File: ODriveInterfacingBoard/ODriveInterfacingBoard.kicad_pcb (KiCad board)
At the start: 2 copper layers, 144.3 x 133.7 mm, 50 parts, among them U1 ODrive, U2 MAX3077E

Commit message: Made LEDs in a Delta Configuration
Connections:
- 50W2RJ1 pad V+: Net-(50W2RJ1-Pad2) -> (no net)
- 50W2RJ1 pad V-: Net-(50W2RJ1-Pad1) -> (no net)
- Conn3 pad 1: PV+ -> /PV+
- Conn4 pad 6: +5V -> /E1_5V
- Conn4 pad 7: +3V3 -> /E1_3V3
- Conn5 pad 6: +5V -> /E0_5V
- Conn5 pad 7: +3V3 -> /E0_3V3
- D12 pad 1: GND -> M0_C
- D13 pad 1: GND -> M1_A
- D15 pad 1: GND -> M0_A
- D5 pad 1: GND -> M1_B
- D8 pad 1: GND -> M0_B
- D9 pad 1: GND -> M1_C
- R1 pad 1: Tx -> GPIO1
- R10 pad 1: PV+ -> M0_C
- R11 pad 1: PV+ -> M1_A
- R14 pad 1: PV+ -> M0_A
- R2 pad 1: Rx -> GPIO2
- R3 pad 1: PV+ -> M1_B
- R6 pad 1: PV+ -> M0_B
- R7 pad 1: PV+ -> M1_C
- U1 pad E0_3V3: +3V3 -> /E0_3V3
- U1 pad E0_5V: +5V -> /E0_5V
- U1 pad E0_GND: GND -> /E0_GND
- U1 pad E1_3V3: +3V3 -> /E1_3V3
- U1 pad E1_5V: +5V -> /E1_5V
- U1 pad E1_GND: GND -> /E1_GND
- U1 pad PV+: PV+ -> (no net)

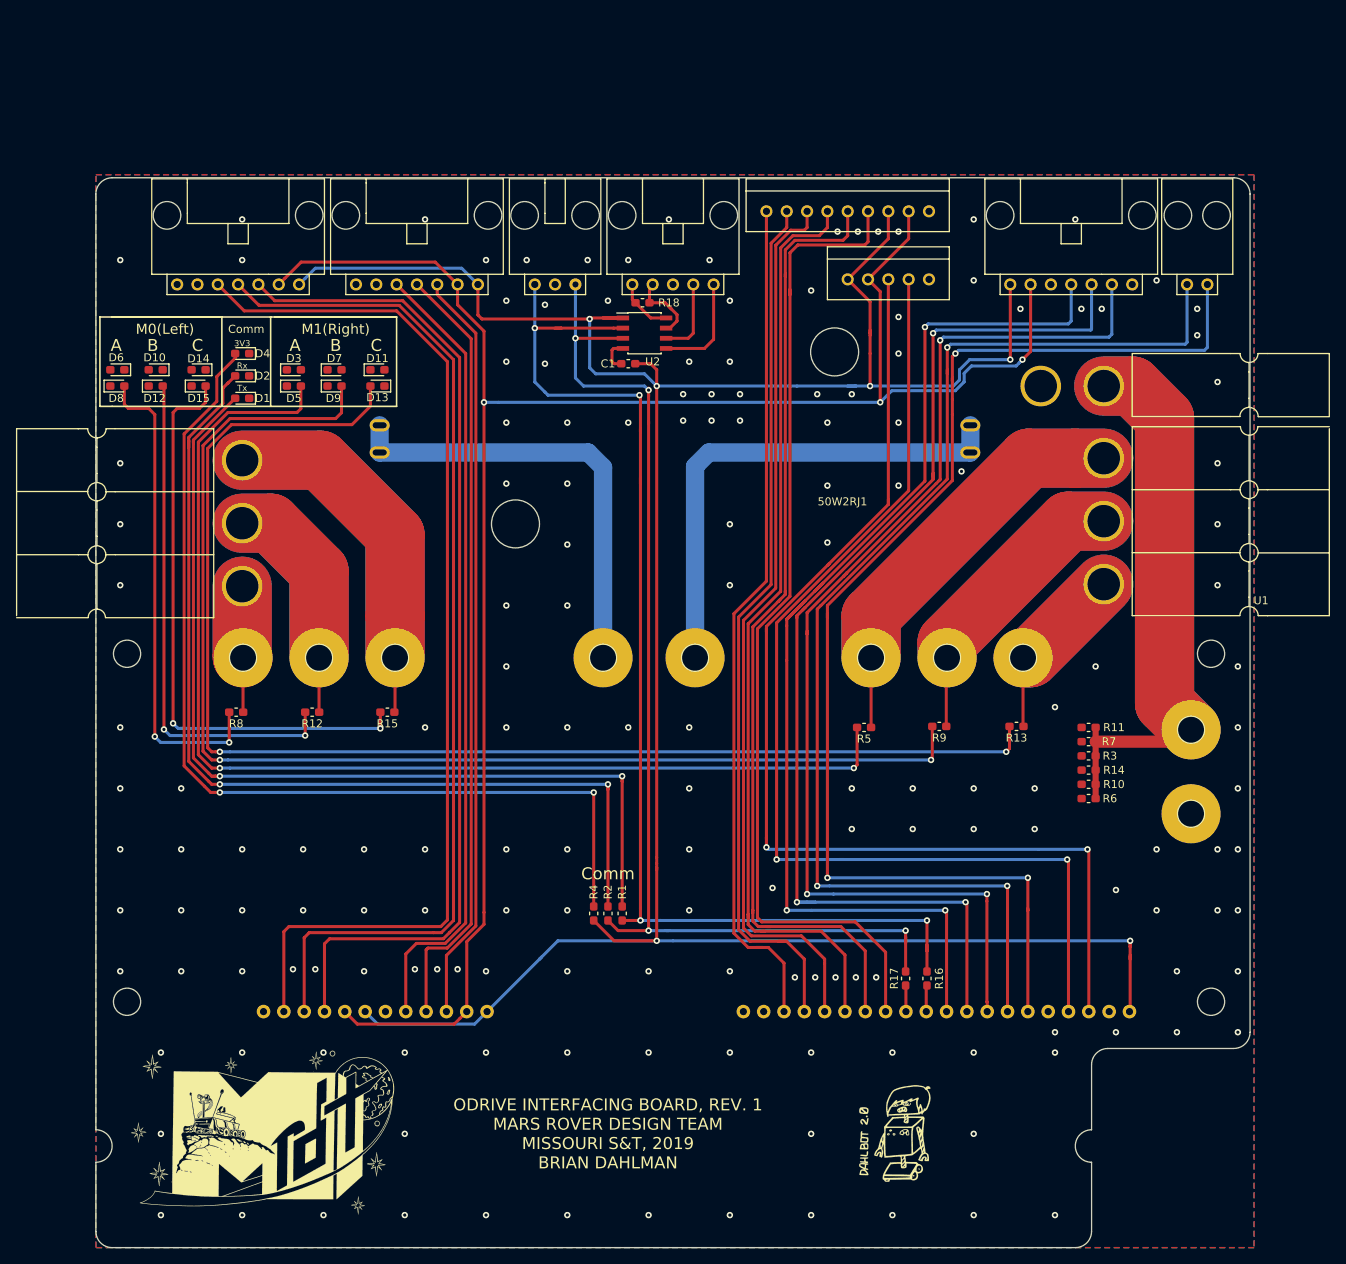
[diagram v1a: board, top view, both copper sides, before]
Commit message: Layout made, functional but needs cleaning up
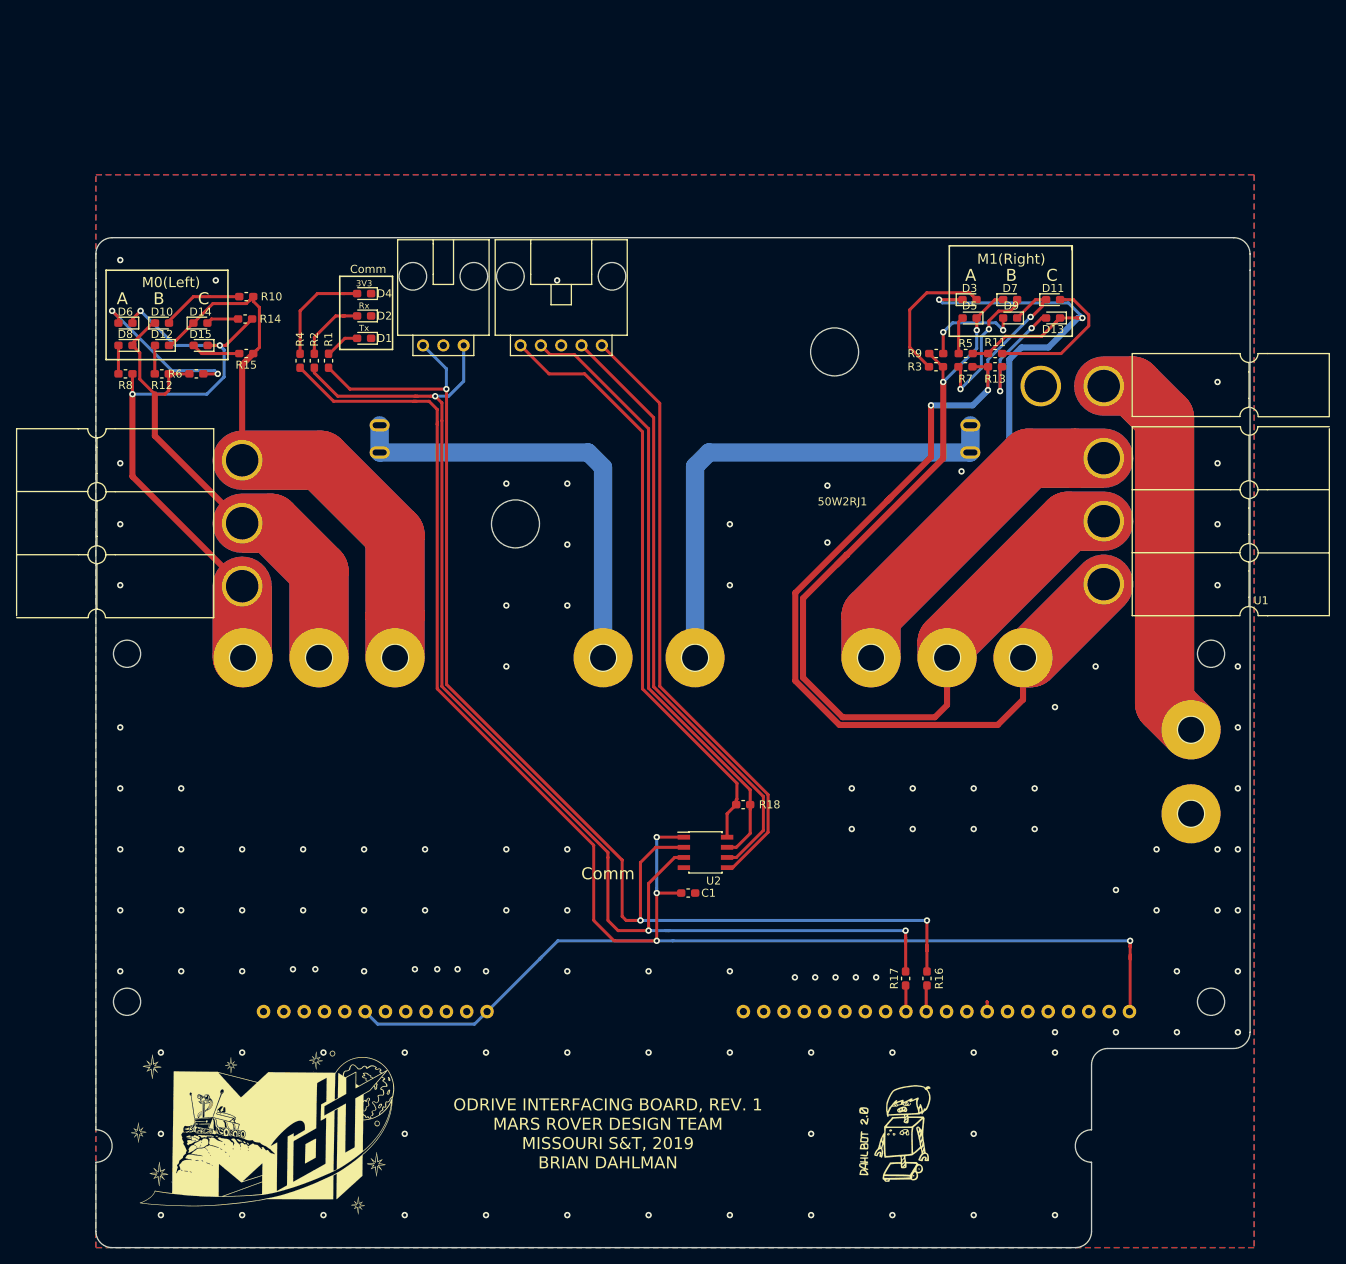
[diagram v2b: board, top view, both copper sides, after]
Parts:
- removed Conn1: Molex_SL_02, MRDT_Connectors:MOLEX_SL_02_Horizontal
- removed Conn13: Molex_SL_09, MRDT_Connectors:MOLEX_SL_09_Vertical
- removed Conn2: Molex_SL_05, MRDT_Connectors:MOLEX_SL_05_Vertical
- removed Conn4, Conn5, Conn6: Molex_SL_07, MRDT_Connectors:MOLEX_SL_07_Horizontal
- moved R6 123.5 mm to (47.6, 65.0), turned to 0 degrees
- moved R10 121.7 mm to (53.8, 55.4)
- moved R14 119.6 mm to (53.7, 58.2)
- moved D3 84.9 mm to (144.3, 55.8)
- moved D7 84.9 mm to (149.3, 55.8)
- moved D11 84.9 mm to (154.7, 55.8)
- moved D5 84.9 mm to (144.3, 58.0), turned to 180 degrees
- moved D9 84.9 mm to (149.3, 58.0), turned to 180 degrees
- moved D13 84.9 mm to (154.7, 58.0)
- moved R1 78.2 mm to (64.1, 63.4)
- moved R2 78.2 mm to (62.4, 63.4)
- moved R4 78.2 mm to (60.6, 63.4)
- moved C1 66.6 mm to (109.1, 129.9), turned to 0 degrees
- moved U2 65.3 mm to (111.3, 124.8)
- moved R18 64.0 mm to (116.0, 118.9)
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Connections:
- 50W2RJ1 pad V+: (no net) -> Net-(50W2RJ1-Pad2)
- 50W2RJ1 pad V-: (no net) -> Net-(50W2RJ1-Pad1)
- Conn3 pad 1: /PV+ -> PV+
- R1 pad 1: GPIO1 -> Tx
- R2 pad 1: GPIO2 -> Rx
- U1 pad E0_3V3: /E0_3V3 -> +3V3
- U1 pad E0_5V: /E0_5V -> +5V
- U1 pad E0_GND: /E0_GND -> GND
- U1 pad E1_3V3: /E1_3V3 -> +3V3
- U1 pad E1_5V: /E1_5V -> +5V
- U1 pad E1_GND: /E1_GND -> GND
- U1 pad PV+: (no net) -> PV+
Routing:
- net +5V: track 240.7 -> 0.00 mm, vias 3 -> 0
- net Net-(Conn1-Pad2): track 154.4 -> 0.00 mm, vias 3 -> 0
- net Net-(Conn1-Pad1): track 151.5 -> 0.00 mm, vias 3 -> 0
- net Net-(D13-Pad2): track 165.8 -> 15.0 mm
- net Net-(D9-Pad2): track 156.3 -> 12.5 mm
- net MISO: track 141.9 -> 0.00 mm, vias 3 -> 0
- net SCK: track 142.2 -> 1.26 mm, vias 3 -> 0
- net MOSI: track 140.4 -> 0.00 mm, vias 3 -> 0
- net Net-(D5-Pad2): track 144.3 -> 4.65 mm, vias 2 -> 0
- net CAN_H: track 139.4 -> 0.00 mm, vias 2 -> 0
- net CAN_L: track 135.3 -> 0.00 mm, vias 2 -> 0
- net /E0_Z: track 133.5 -> 0.00 mm
- net /E0_B: track 129.7 -> 0.00 mm
- net /E0_A: track 126.0 -> 0.00 mm
- net GPIO_3: track 124.8 -> 0.00 mm
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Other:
- board size 144.3 x 133.7 mm -> 144.3 x 126.2 mm

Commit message: started reworking the leds
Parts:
- removed C1: .1u, Capacitor_SMD:C_0603_1608Metric_Pad1.05x0.95mm_HandSolder
- removed Conn10: Molex_SL_05, MRDT_Connectors:MOLEX_SL_05_Horizontal
- removed R18: 120, Resistor_SMD:R_0603_1608Metric_Pad1.05x0.95mm_HandSolder
- removed U2: MAX3077E, Package_SO:SOIC-8_3.9x4.9mm_P1.27mm
- moved D12 34.1 mm to (47.6, 27.7)
- moved D10 34.1 mm to (47.6, 24.9)
- moved D14 34.1 mm to (52.4, 24.9)
- moved R10 34.1 mm to (58.2, 21.6)
- moved R12 34.1 mm to (47.6, 31.2)
- moved R6 34.1 mm to (51.9, 31.2)
- moved R3 30.8 mm to (138.3, 33.4)
- moved R9 30.8 mm to (138.3, 31.8)
- moved R7 30.2 mm to (144.3, 33.9)
- moved R5 30.2 mm to (144.3, 32.3)
- moved Conn9 27.2 mm to (105.7, 61.5)
- moved D1 24.5 mm to (93.0, 57.8)
- moved D2 24.5 mm to (93.0, 55.0)
- moved D4 24.5 mm to (93.0, 52.2)
- moved R1 24.5 mm to (88.5, 60.6)
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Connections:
- Conn3 pad 1: PV+ -> /PV+
- U1 pad E0_5V: +5V -> /E0_5V
- U1 pad E0_GND: GND -> /E0_GND
- U1 pad E1_5V: +5V -> /E1_5V
- U1 pad E1_GND: GND -> /E1_GND
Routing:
- net PV+: track 101.3 -> 0.00 mm
- net /PV+: track 0.00 -> 101.3 mm
- net Net-(Conn10-Pad2): track 77.2 -> 0.00 mm
- net Net-(Conn10-Pad5): track 76.4 -> 0.00 mm
- net Net-(Conn10-Pad4): track 76.0 -> 0.00 mm
- net Net-(Conn10-Pad1): track 75.8 -> 0.00 mm
- net M1_A: track 147.7 -> 88.4 mm, vias 2 -> 0
- net M0_A: track 87.1 -> 47.5 mm, vias 3 -> 1
- net M1_C: track 139.2 -> 100.7 mm, vias 3 -> 0
- net M0_C: track 111.4 -> 76.9 mm
- net +3V3: track 230.9 -> 200.9 mm
- net Tx: track 159.7 -> 132.7 mm, vias 3 -> 2
- net Net-(D6-Pad2): track 20.1 -> 0.00 mm, vias 2 -> 0
- net Rx: track 159.6 -> 139.6 mm
- net M1_B: track 146.7 -> 128.4 mm, vias 2 -> 1
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
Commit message: schematic work
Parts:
- moved R10 37.9 mm to (44.2, 56.8), turned to 90 degrees
- moved R8 26.0 mm to (67.3, 44.8)
- moved D15 24.6 mm to (63.8, 48.4)
- moved D10 12.5 mm to (48.7, 37.3)
- moved D14 12.5 mm to (53.5, 37.3)
- moved R12 12.5 mm to (48.6, 43.7)
- moved R6 12.5 mm to (52.9, 43.7)
- moved D12 12.5 mm to (48.7, 40.1)
- moved R14 5.58 mm to (46.0, 56.8)
- moved D8 3.56 mm to (42.4, 56.8), turned to 270 degrees
- moved D6 1.78 mm to (40.6, 56.8)
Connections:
- 50W2RJ1 pad V+: Net-(50W2RJ1-Pad2) -> (no net)
- 50W2RJ1 pad V-: Net-(50W2RJ1-Pad1) -> (no net)
- D12 pad 1: M0_C -> Net-(D10-Pad2)
- D12 pad 2: Net-(D12-Pad2) -> M0_B
- D13 pad 1: M1_A -> Net-(D11-Pad2)
- D13 pad 2: Net-(D13-Pad2) -> M1_C
- D15 pad 1: M0_A -> Net-(D14-Pad2)
- D15 pad 2: Net-(D15-Pad2) -> M0_C
- D5 pad 1: M1_B -> Net-(D3-Pad2)
- D5 pad 2: Net-(D5-Pad2) -> M1_A
- D8 pad 1: M0_B -> Net-(D6-Pad2)
- D8 pad 2: Net-(D8-Pad2) -> M0_A
- D9 pad 1: M1_C -> Net-(D7-Pad2)
- D9 pad 2: Net-(D9-Pad2) -> M1_B
- R1 pad 1: Tx -> GPIO1
- R10 pad 1: M0_C -> M0_A
- R10 pad 2: Net-(D10-Pad2) -> Net-(D14-Pad2)
- R2 pad 1: Rx -> GPIO2
- R8 pad 1: M0_A -> M0_C
- R8 pad 2: Net-(D8-Pad2) -> Net-(D10-Pad2)
- R9 pad 1: M1_B -> M1_A
- R9 pad 2: Net-(D9-Pad2) -> Net-(D11-Pad2)
- U1 pad E0_3V3: +3V3 -> /E0_3V3
- U1 pad E1_3V3: +3V3 -> /E1_3V3
- U1 pad PV+: PV+ -> (no net)
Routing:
- net Net-(D8-Pad2): track 0.58 -> 0.00 mm

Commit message: leds almost done
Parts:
- removed R12, R13, R14, R15, R5, R9: 1.5k, Resistor_SMD:R_0603_1608Metric_Pad1.05x0.95mm_HandSolder
- moved R11 79.9 mm to (67.8, 56.5), turned to 90 degrees
- moved R3 67.9 mm to (74.4, 56.5), turned to 90 degrees
- moved D3 67.6 mm to (69.8, 56.5), turned to 90 degrees
- moved R7 67.2 mm to (81.0, 56.5), turned to 90 degrees
- moved D7 66.0 mm to (76.5, 56.5), turned to 90 degrees
- moved D5 65.5 mm to (71.9, 56.5), turned to 270 degrees
- moved D11 64.8 mm to (83.1, 56.5), turned to 90 degrees
- moved D9 64.0 mm to (78.5, 56.5), turned to 270 degrees
- moved D13 62.8 mm to (85.1, 56.5), turned to 270 degrees
- moved D4 32.7 mm to (60.6, 56.5), turned to 270 degrees
- moved D2 30.6 mm to (62.4, 56.5), turned to 270 degrees
- moved D1 28.9 mm to (64.1, 56.5), turned to 270 degrees
- moved R1 24.4 mm to (64.1, 62.1)
- moved R2 24.4 mm to (62.4, 62.1)
- moved R4 24.4 mm to (60.6, 62.1)
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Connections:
- R1 pad 1: GPIO1 -> Tx
- R2 pad 1: GPIO2 -> Rx
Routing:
- net M1_A: track 88.4 -> 206.4 mm, vias 0 -> 2
- net M1_C: track 100.7 -> 154.0 mm, vias 0 -> 1
- net M1_B: track 128.4 -> 181.4 mm, vias 1 -> 2
- net +3V3: track 200.9 -> 230.1 mm
- net Tx: track 132.7 -> 157.8 mm
- net Rx: track 139.6 -> 163.8 mm
- net M0_C: track 76.7 -> 99.2 mm
- net Net-(D14-Pad2): track 0.00 -> 19.2 mm
- net Net-(D11-Pad2): track 0.62 -> 19.3 mm
- net M0_B: track 66.5 -> 82.3 mm
- net M0_A: track 47.5 -> 61.7 mm, vias 1 -> 0
- net Net-(D4-Pad2): track 13.7 -> 3.84 mm
- net Net-(D2-Pad2): track 8.78 -> 3.84 mm
- net Net-(D6-Pad2): track 0.00 -> 4.58 mm
- net Net-(D7-Pad2): track 0.00 -> 4.57 mm
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
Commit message: Finished the layout.
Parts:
- moved R16 0.06 mm to (138.9, 140.6)
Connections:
- 50W2RJ1 pad V+: (no net) -> Net-(50W2RJ1-Pad2)
- 50W2RJ1 pad V-: (no net) -> Net-(50W2RJ1-Pad1)
- U1 pad E0_3V3: /E0_3V3 -> +3V3
- U1 pad E1_3V3: /E1_3V3 -> +3V3
- U1 pad PV+: (no net) -> /PV+
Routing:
- net +3V3: track 230.1 -> 232.7 mm
- net Tx: track 157.8 -> 156.9 mm
- net GND: vias 108 -> 141
- net (no net): vias 1 -> 0
